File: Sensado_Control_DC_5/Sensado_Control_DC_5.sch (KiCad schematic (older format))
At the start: 110 parts, among them J1 Jumper, J2 Jumper, J3 Jumper, P1 R_FUENTE_CON, P10 GPIO, P11 TOR_4, P12 TOR_2, P13 TOR_1, P14 TOR_3, P15 J_RESET, P2 I_+, P3 I_-, P4 POWER, P5 RS-232, P6 I2C, P7 SPI, P8 GND_REG, P9 RESET, Q1 NMOS, Q10 PMOS, Q11 NMOS, Q12 NMOS, Q13 NMOS, Q14 PMOS, Q15 PMOS, Q16 PMOS, Q2 NMOS, Q3 NMOS, Q4 NMOS, Q5 NMOS, Q6 PMOS, Q7 PMOS, Q8 PMOS, Q9 PMOS, U1 Atmega328PA, U2 ACS_712, U3 LD1117S50TR_FINAL, Y1 XRCHA_16M

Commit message: Archivo .zip actualizado de Gerbers
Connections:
- net AGND: now reaches P15.1 (P1)
- no-connect marks 7 -> 6
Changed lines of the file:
@@
 	1    0    0    -1
 $EndComp
-NoConn ~ 6150 4220
+Wire Wire Line
+	6150 4220 6030 4220
+Text Label 6030 4220 0    39   ~ 0
+AGND
 $EndSCHEMATC

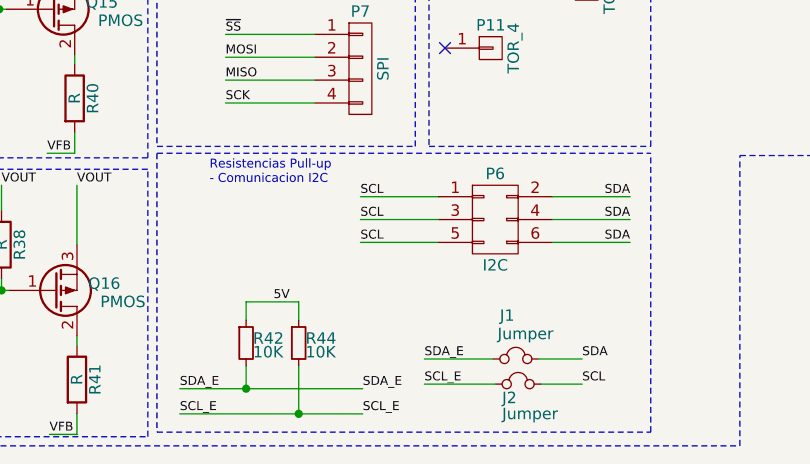
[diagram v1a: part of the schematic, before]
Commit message: Resistencias de pull up quitadas
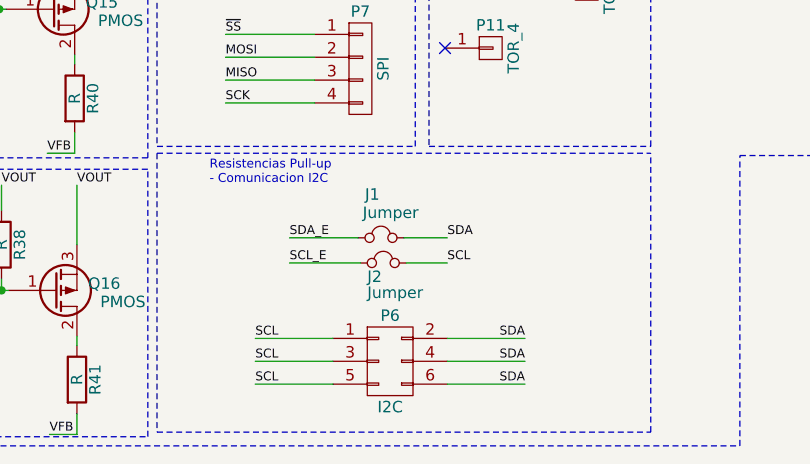
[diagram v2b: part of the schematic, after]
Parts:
- removed R42, R44: 10K, Resistors_SMD:R_0805_HandSoldering, symbol 10K
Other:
- moved on the sheet: J1, J2, P6
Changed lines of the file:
@@
 Text Label 4630 6250 0    39   ~ 0
 SCK
-Text Label 6400 6760 2    39   ~ 0
+Text Label 5940 7380 2    39   ~ 0
 SDA
-Text Label 5220 6760 0    39   ~ 0
+Text Label 4760 7380 0    39   ~ 0
 SCL
 Text Notes 4560 6610 0    39   ~ 0
 Resistencias Pull-up\n- Comunicacion I2C
-Text Label 4430 7500 0    39   ~ 0
-SDA_E
-Text Label 4430 7610 0    39   ~ 0
-SCL_E
-Text Label 5230 7500 0    39   ~ 0
-SDA_E
-Text Label 5230 7610 0    39   ~ 0
-SCL_E
 $Comp
 L Jumper J1
 U 1 1 59DB5A77
-P 5900 7370
-F 0 "J1" V 5710 7300 50  0000 L CNN
-F 1 "Jumper" V 5790 7290 50  0000 L CNN
-F 2 "Pin_Headers:Pin_Header_Straight_1x02_Pitch2.54mm" H 5900 7370 50  0001 C CNN
-F 3 "" H 5900 7370 50  0000 C CNN
-	1    5900 7370
+P 5310 6840
+F 0 "J1" V 5120 6770 50  0000 L CNN
+F 1 "Jumper" V 5200 6760 50  0000 L CNN
+F 2 "Pin_Headers:Pin_Header_Straight_1x02_Pitch2.54mm" H 5310 6840 50  0001 C CNN
+F 3 "" H 5310 6840 50  0000 C CNN
+	1    5310 6840
 	0    1    1    0
 $EndComp
@@
 L Jumper J2
 U 1 1 59DB5B56
-P 5910 7480
-F 0 "J2" V 5970 7410 50  0000 L CNN
-F 1 "Jumper" V 6040 7410 50  0000 L CNN
-F 2 "Pin_Headers:Pin_Header_Straight_1x02_Pitch2.54mm" H 5910 7480 50  0001 C CNN
-F 3 "" H 5910 7480 50  0000 C CNN
-	1    5910 7480
+P 5320 6950
+F 0 "J2" V 5380 6880 50  0000 L CNN
+F 1 "Jumper" V 5450 6880 50  0000 L CNN
+F 2 "Pin_Headers:Pin_Header_Straight_1x02_Pitch2.54mm" H 5320 6950 50  0001 C CNN
+F 3 "" H 5320 6950 50  0000 C CNN
+	1    5320 6950
 	0    1    1    0
 $EndComp
-Text Label 5500 7370 0    39   ~ 0
+Text Label 4910 6840 0    39   ~ 0
 SDA_E
-Text Label 5500 7480 0    39   ~ 0
+Text Label 4910 6950 0    39   ~ 0
 SCL_E
-Text Label 6190 7370 0    39   ~ 0
+Text Label 5600 6840 0    39   ~ 0
 SDA
-Text Label 6190 7480 0    39   ~ 0
+Text Label 5600 6950 0    39   ~ 0
 SCL
 Text Label 4350 660  0    39   ~ 0
@@
 Text Notes 6120 4060 0    39   ~ 0
 Reset Micro
-Text Label 4840 7120 0    39   ~ 0
-5V
-$Comp
-L 10K R42
-U 1 1 59D27397
-P 4720 7300
-F 0 "R42" H 4750 7320 50  0000 L CNN
-F 1 "10K" H 4750 7260 50  0000 L CNN
-F 2 "Resistors_SMD:R_0805_HandSoldering" H 4650 7220 50  0001 C CNN
-F 3 "" H 4720 7300 50  0000 C CNN
-F 4 "RMCF0805FT10K0TR-ND" H 4850 7420 39  0001 C CNN "RES SMD 10K OHM 1% 1/8W 0805"
-	1    4720 7300
-	1    0    0    -1
-$EndComp
-$Comp
-L 10K R44
-U 1 1 59D27507
-P 4950 7300
-F 0 "R44" H 4980 7320 50  0000 L CNN
-F 1 "10K" H 4980 7260 50  0000 L CNN
-F 2 "Resistors_SMD:R_0805_HandSoldering" H 4880 7220 50  0001 C CNN
-F 3 "" H 4950 7300 50  0000 C CNN
-F 4 "RMCF0805FT10K0TR-ND" H 5080 7420 39  0001 C CNN "RES SMD 10K OHM 1% 1/8W 0805"
-	1    4950 7300
-	1    0    0    -1
-$EndComp
 $Comp
 L 1nF_THT C4
@@
 	4330 6470 6490 6470
 Wire Wire Line
-	6060 6760 6400 6760
-Wire Wire Line
-	5560 6760 5220 6760
+	5600 7380 5940 7380
+Wire Wire Line
+	5100 7380 4760 7380
 Wire Notes Line
 	4330 6470 4330 7690
 Wire Wire Line
-	4720 7120 4720 7200
-Wire Wire Line
-	4720 7120 4950 7120
-Wire Wire Line
-	4950 7120 4950 7200
-Wire Wire Line
-	4720 7400 4720 7500
-Wire Wire Line
-	4430 7500 5230 7500
-Connection ~ 4720 7500
-Wire Wire Line
-	4950 7400 4950 7610
-Wire Wire Line
-	4430 7610 5230 7610
-Connection ~ 4950 7610
-Wire Wire Line
-	5500 7370 5800 7370
-Wire Wire Line
-	5500 7480 5810 7480
-Wire Wire Line
-	6000 7370 6190 7370
-Wire Wire Line
-	6010 7480 6190 7480
+	4910 6840 5210 6840
+Wire Wire Line
+	4910 6950 5220 6950
+Wire Wire Line
+	5410 6840 5600 6840
+Wire Wire Line
+	5420 6950 5600 6950
 Wire Notes Line
 	4330 7690 6490 7690
@@
 L CONN_02X03 P6
 U 1 1 59D41214
-P 5810 6760
-F 0 "P6" H 5810 6960 50  0000 C CNN
-F 1 "I2C" H 5810 6560 50  0000 C CNN
-F 2 "Socket_Strips:Socket_Strip_Straight_2x03_Pitch2.54mm" H 5810 5560 50  0001 C CNN
-F 3 "" H 5810 5560 50  0000 C CNN
-	1    5810 6760
-	1    0    0    -1
-$EndComp
-Text Label 5220 6660 0    39   ~ 0
+P 5350 7380
+F 0 "P6" H 5350 7580 50  0000 C CNN
+F 1 "I2C" H 5350 7180 50  0000 C CNN
+F 2 "Socket_Strips:Socket_Strip_Straight_2x03_Pitch2.54mm" H 5350 6180 50  0001 C CNN
+F 3 "" H 5350 6180 50  0000 C CNN
+	1    5350 7380
+	1    0    0    -1
+$EndComp
+Text Label 4760 7280 0    39   ~ 0
 SCL
 Wire Wire Line
-	5560 6660 5220 6660
-Text Label 5220 6860 0    39   ~ 0
+	5100 7280 4760 7280
+Text Label 4760 7480 0    39   ~ 0
 SCL
 Wire Wire Line
-	5560 6860 5220 6860
-Text Label 6400 6660 2    39   ~ 0
+	5100 7480 4760 7480
+Text Label 5940 7280 2    39   ~ 0
 SDA
 Wire Wire Line
-	6060 6660 6400 6660
-Text Label 6400 6860 2    39   ~ 0
+	5600 7280 5940 7280
+Text Label 5940 7480 2    39   ~ 0
 SDA
 Wire Wire Line
-	6060 6860 6400 6860
+	5600 7480 5940 7480
 Wire Notes Line
 	6490 7690 6490 6470

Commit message: Capacitor del Cristal 0402 cambiados
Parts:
- C7, C8: footprint Capacitors_SMD:C_0805_HandSoldering -> Capacitors_SMD:C_0402
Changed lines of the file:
@@
 F 0 "C8" H 6520 3690 50  0000 L CNN
 F 1 "8pF" H 6520 3540 50  0000 L CNN
-F 2 "Capacitors_SMD:C_0805_HandSoldering" H 6420 3590 50  0001 C CNN
+F 2 "Capacitors_SMD:C_0402" H 6420 3590 50  0001 C CNN
 F 3 "" H 6520 3690 50  0000 C CNN
 F 4 "399-1113-2-ND" H 6620 3790 39  0001 C CNN "CAP CER 22PF 50V C0G/NP0 0805"
@@
 F 0 "C7" H 5750 3660 50  0000 L CNN
 F 1 "8pF" H 5750 3510 50  0000 L CNN
-F 2 "Capacitors_SMD:C_0805_HandSoldering" H 5650 3560 50  0001 C CNN
+F 2 "Capacitors_SMD:C_0402" H 5650 3560 50  0001 C CNN
 F 3 "" H 5750 3660 50  0000 C CNN
 F 4 "399-1113-2-ND" H 5850 3760 39  0001 C CNN "CAP CER 22PF 50V C0G/NP0 0805"
